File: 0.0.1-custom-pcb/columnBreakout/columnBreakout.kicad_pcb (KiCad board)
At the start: 2 copper layers, 14 x 63 mm, 7 parts, among them J1 HC-FPC-0.5-12P-FH20, J2 HC-FPC-0.5-6P-FH20, J3 HC-FPC-0.5-6P-FH20, J4 HC-FPC-0.5-6P-FH20, J5 HC-FPC-0.5-6P-FH20, J6 HC-FPC-0.5-6P-FH20, J7 HC-FPC-0.5-6P-FH20

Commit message: final work before codex review
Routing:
- net /R3: track 36.9 -> 27.3 mm
- net /R0: track 62.2 -> 55.2 mm
- net /R4: track 24.9 -> 19.0 mm, vias 2 -> 0
- net /R1: track 50.9 -> 45.9 mm
- net /R2: track 39.7 -> 36.7 mm
- net /R5: track 12.5 -> 9.53 mm, vias 2 -> 0
- net /IN0: track 58.0 -> 55.0 mm
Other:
- board size 14 x 63 mm -> 12 x 63 mm
- board text added: "columnBreakout Rev 1"

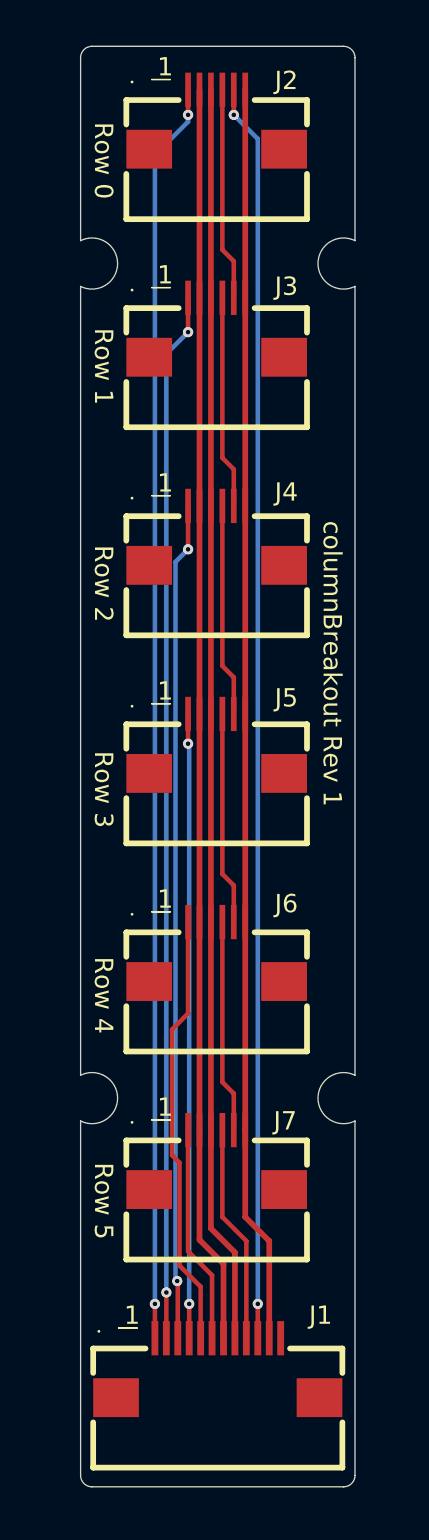
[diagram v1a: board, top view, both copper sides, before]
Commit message: make borders square and use dot as pin 1 marker
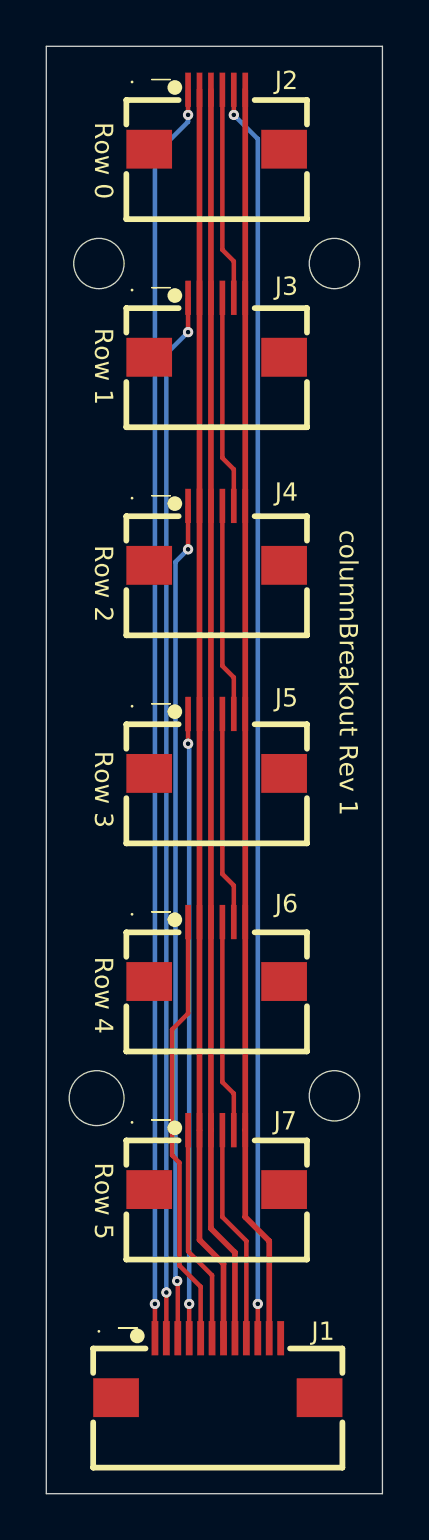
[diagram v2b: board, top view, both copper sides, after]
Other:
- board size 12 x 63 mm -> 14.7 x 63.3 mm
- board text removed: "1"
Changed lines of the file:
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@@
 		(at 154 99.8)
 		(property "Reference" "J1"
-			(at 4.5 -2.3 0)
+			(at 4.6 -1.6 0)
 			(layer "F.SilkS")
 			(effects
@@
 		)
 	)
-	(gr_arc
-		(start 148 42.5)
-		(mid 148.146447 42.146447)
-		(end 148.5 42)
+	(gr_circle
+		(center 150.478925 98.4)
+		(end 150.8 98.4)
+		(stroke
+			(width 0)
+			(type solid)
+		)
+		(fill yes)
+		(layer "F.SilkS")
+	)
+	(gr_circle
+		(center 152.121075 43.8)
+		(end 152.44215 43.8)
+		(stroke
+			(width 0)
+			(type solid)
+		)
+		(fill yes)
+		(layer "F.SilkS")
+	)
+	(gr_circle
+		(center 152.121075 52.9)
+		(end 152.44215 52.9)
+		(stroke
+			(width 0)
+			(type solid)
+		)
+		(fill yes)
+		(layer "F.SilkS")
+	)
+	(gr_circle
+		(center 152.121075 62)
+		(end 152.44215 62)
+		(stroke
+			(width 0)
+			(type solid)
+		)
+		(fill yes)
+		(layer "F.SilkS")
+	)
+	(gr_circle
+		(center 152.121075 71.1)
+		(end 152.44215 71.1)
+		(stroke
+			(width 0)
+			(type solid)
+		)
+		(fill yes)
+		(layer "F.SilkS")
+	)
+	(gr_circle
+		(center 152.121075 80.2)
+		(end 152.44215 80.2)
+		(stroke
+			(width 0)
+			(type solid)
+		)
+		(fill yes)
+		(layer "F.SilkS")
+	)
+	(gr_circle
+		(center 152.121075 89.3)
+		(end 152.44215 89.3)
+		(stroke
+			(width 0)
+			(type solid)
+		)
+		(fill yes)
+		(layer "F.SilkS")
+	)
+	(gr_line
+		(start 146.5 42)
+		(end 161.2 42)
 		(stroke
 			(width 0.05)
@@
 	)
 	(gr_line
-		(start 148 50.500002)
-		(end 148 42.5)
+		(start 146.5 105.3)
+		(end 146.5 42)
 		(stroke
 			(width 0.05)
@@
 		(layer "Edge.Cuts")
 	)
-	(gr_arc
-		(start 148 50.5)
-		(mid 149.618034 51.5)
-		(end 148 52.5)
+	(gr_circle
+		(center 148.7 88)
+		(end 149.9 88)
 		(stroke
 			(width 0.05)
 			(type default)
 		)
+		(fill no)
 		(layer "Edge.Cuts")
 	)
-	(gr_line
-		(start 148 87.000002)
-		(end 148 52.5)
+	(gr_circle
+		(center 148.8 51.5)
+		(end 147.7 51.5)
 		(stroke
 			(width 0.05)
 			(type default)
 		)
+		(fill no)
 		(layer "Edge.Cuts")
 	)
-	(gr_arc
-		(start 148 87)
-		(mid 149.618034 88)
-		(end 148 89)
+	(gr_circle
+		(center 159.1 51.5)
+		(end 160.2 51.5)
 		(stroke
 			(width 0.05)
 			(type default)
 		)
+		(fill no)
 		(layer "Edge.Cuts")
 	)
-	(gr_line
-		(start 148 104.5)
-		(end 148 89)
+	(gr_circle
+		(center 159.1 87.9)
+		(end 160.2 87.9)
 		(stroke
 			(width 0.05)
 			(type default)
 		)
+		(fill no)
 		(layer "Edge.Cuts")
 	)
 	(gr_line
-		(start 148.5 42)
-		(end 159.5 42)
+		(start 161.2 42)
+		(end 161.2 105.3)
 		(stroke
 			(width 0.05)
@@
 		(layer "Edge.Cuts")
 	)
-	(gr_arc
-		(start 148.5 105)
-		(mid 148.146447 104.853553)
-		(end 148 104.5)
+	(gr_line
+		(start 161.2 105.3)
+		(end 146.5 105.3)
 		(stroke
 			(width 0.05)
@@
 		)
 		(layer "Edge.Cuts")
-	)
-	(gr_arc
-		(start 159.5 42)
-		(mid 159.853553 42.146447)
-		(end 160 42.5)
-		(stroke
-			(width 0.05)
-			(type default)
-		)
-		(layer "Edge.Cuts")
-	)
-	(gr_line
-		(start 159.5 105)
-		(end 148.5 105)
-		(stroke
-			(width 0.05)
-			(type default)
-		)
-		(layer "Edge.Cuts")
-	)
-	(gr_line
-		(start 160 50.5)
-		(end 160 42.5)
-		(stroke
-			(width 0.05)
-			(type default)
-		)
-		(layer "Edge.Cuts")
-	)
-	(gr_arc
-		(start 160 52.5)
-		(mid 158.381966 51.5)
-		(end 160 50.5)
-		(stroke
-			(width 0.05)
-			(type default)
-		)
-		(layer "Edge.Cuts")
-	)
-	(gr_line
-		(start 160 87)
-		(end 160 52.5)
-		(stroke
-			(width 0.05)
-			(type default)
-		)
-		(layer "Edge.Cuts")
-	)
-	(gr_arc
-		(start 160 89)
-		(mid 158.381966 88)
-		(end 160 87)
-		(stroke
-			(width 0.05)
-			(type default)
-		)
-		(layer "Edge.Cuts")
-	)
-	(gr_line
-		(start 160 89)
-		(end 160 104.5)
-		(stroke
-			(width 0.05)
-			(type default)
-		)
-		(layer "Edge.Cuts")
-	)
-	(gr_arc
-		(start 160 104.5)
-		(mid 159.853553 104.853553)
-		(end 159.5 105)
-		(stroke
-			(width 0.05)
-			(type default)
-		)
-		(layer "Edge.Cuts")
-	)
-	(gr_text "1"
-		(at 150.25 97.5 0)
-		(layer "F.SilkS")
-		(effects
-			(font
-				(size 0.8 0.8)
-				(thickness 0.12)
-			)
-		)
-	)
-	(gr_text "1"
-		(at 151.7 42.9 0)
-		(layer "F.SilkS")
-		(effects
-			(font
-				(size 0.8 0.8)
-				(thickness 0.12)
-			)
-		)
-	)
-	(gr_text "1"
-		(at 151.7 52 0)
-		(layer "F.SilkS")
-		(effects
-			(font
-				(size 0.8 0.8)
-				(thickness 0.12)
-			)
-		)
-	)
-	(gr_text "1"
-		(at 151.7 61.1 0)
-		(layer "F.SilkS")
-		(effects
-			(font
-				(size 0.8 0.8)
-				(thickness 0.12)
-			)
-		)
-	)
-	(gr_text "1"
-		(at 151.7 70.2 0)
-		(layer "F.SilkS")
-		(effects
-			(font
-				(size 0.8 0.8)
-				(thickness 0.12)
-			)
-		)
-	)
-	(gr_text "1"
-		(at 151.7 79.3 0)
-		(layer "F.SilkS")
-		(effects
-			(font
-				(size 0.8 0.8)
-				(thickness 0.12)
-			)
-		)
-	)
-	(gr_text "1"
-		(at 151.7 88.4 0)
-		(layer "F.SilkS")
-		(effects
-			(font
-				(size 0.8 0.8)
-				(thickness 0.12)
-			)
-		)
 	)
 	(gr_text "Row 0"
@@
 	)
 	(gr_text "columnBreakout Rev 1"
-		(at 159 69 270)
+		(at 159.7 69.4 270)
 		(layer "F.SilkS")
 		(effects

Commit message: final changes to columnBreakout
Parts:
- added H1: MountingHole_2.2mm_M2_4.4mmHead, Mechanical:MountingHole_2.2mm_M2_4.4mmHead, F.Cu at (148.8, 51.5)
- added H2: MountingHole_2.2mm_M2_4.4mmHead, Mechanical:MountingHole_2.2mm_M2_4.4mmHead, F.Cu at (159.1, 51.5)
- added H3: MountingHole_2.2mm_M2_4.4mmHead, Mechanical:MountingHole_2.2mm_M2_4.4mmHead, F.Cu at (148.8, 87.9)
- added H4: MountingHole_2.2mm_M2_4.4mmHead, Mechanical:MountingHole_2.2mm_M2_4.4mmHead, F.Cu at (159.1, 87.9)
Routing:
- net /R0: track 55.2 -> 64.1 mm
- net /VDD: track 55.0 -> 61.1 mm, vias 0 -> 7
- net /GND: track 55.0 -> 60.9 mm, vias 0 -> 7
- net /R3: track 27.3 -> 28.0 mm, vias 2 -> 0
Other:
- outline, holes or cut-outs redrawn
